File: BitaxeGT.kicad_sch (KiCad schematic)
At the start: 10 parts, among them J1 XT30

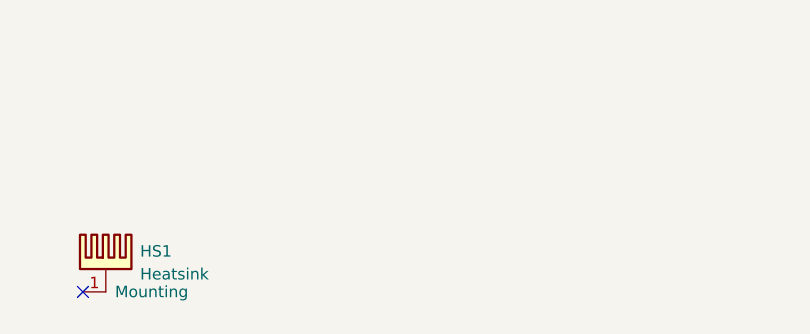
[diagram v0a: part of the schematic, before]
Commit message: add TCH logo
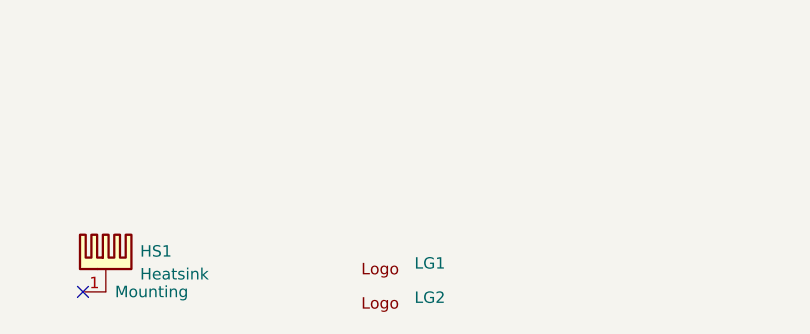
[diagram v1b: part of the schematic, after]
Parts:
- added LG1: ~, TinyChipHub:TCH-Logo, symbol TinyChipHub:TCH_Logo
- added LG2: ~, TinyChipHub:TCH-Logo-Mask, symbol TinyChipHub:TCH_Logo
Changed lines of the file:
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@@
+	)
+	(symbol
+		(lib_id "TinyChipHub:TCH_Logo")
+		(at 149.86 186.69 0)
+		(unit 1)
+		(exclude_from_sim no)
+		(in_bom yes)
+		(on_board yes)
+		(dnp no)
+		(fields_autoplaced yes)
+		(property "Reference" "LG1"
+			(at 153.67 187.3249 0)
+			(effects
+				(font
+					(size 1.27 1.27)
+				)
+				(justify left)
+			)
+		)
+		(property "Value" "~"
+			(at 153.67 189.23 0)
+			(effects
+				(font
+					(size 1.27 1.27)
+				)
+				(justify left)
+			)
+		)
+		(property "Footprint" "TinyChipHub:TCH-Logo"
+			(at 149.86 186.69 0)
+			(effects
+				(font
+					(size 1.27 1.27)
+				)
+				(hide yes)
+			)
+		)
+		(property "Datasheet" ""
+			(at 149.86 186.69 0)
+			(effects
+				(font
+					(size 1.27 1.27)
+				)
+				(hide yes)
+			)
+		)
+		(property "Description" ""
+			(at 149.86 186.69 0)
+			(effects
+				(font
+					(size 1.27 1.27)
+				)
+				(hide yes)
+			)
+		)
+		(instances
+			(project ""
+				(path "/61fe8d2c-9301-4ad9-8caf-c47acfa835b0"
+					(reference "LG1")
+					(unit 1)
+				)
+			)
+		)
+	)
+	(symbol
+		(lib_id "TinyChipHub:TCH_Logo")
+		(at 149.86 190.5 0)
+		(unit 1)
+		(exclude_from_sim no)
+		(in_bom yes)
+		(on_board yes)
+		(dnp no)
+		(fields_autoplaced yes)
+		(property "Reference" "LG2"
+			(at 153.67 191.1349 0)
+			(effects
+				(font
+					(size 1.27 1.27)
+				)
+				(justify left)
+			)
+		)
+		(property "Value" "~"
+			(at 153.67 193.04 0)
+			(effects
+				(font
+					(size 1.27 1.27)
+				)
+				(justify left)
+			)
+		)
+		(property "Footprint" "TinyChipHub:TCH-Logo-Mask"
+			(at 149.86 190.5 0)
+			(effects
+				(font
+					(size 1.27 1.27)
+				)
+				(hide yes)
+			)
+		)
+		(property "Datasheet" ""
+			(at 149.86 190.5 0)
+			(effects
+				(font
+					(size 1.27 1.27)
+				)
+				(hide yes)
+			)
+		)
+		(property "Description" ""
+			(at 149.86 190.5 0)
+			(effects
+				(font
+					(size 1.27 1.27)
+				)
+				(hide yes)
+			)
+		)
+		(instances
+			(project "BitaxeGT"
+				(path "/61fe8d2c-9301-4ad9-8caf-c47acfa835b0"
+					(reference "LG2")
+					(unit 1)
+				)
+			)
+		)
 	)
 	(symbol
